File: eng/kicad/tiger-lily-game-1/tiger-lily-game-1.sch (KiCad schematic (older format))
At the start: 11 parts, among them J1 Conn_01x06_Male, SW1 SW_Push, SW2 SW_Push, SW3 SW_Push, SW4 SW_SPDT, U1 PIC16F1454-IP

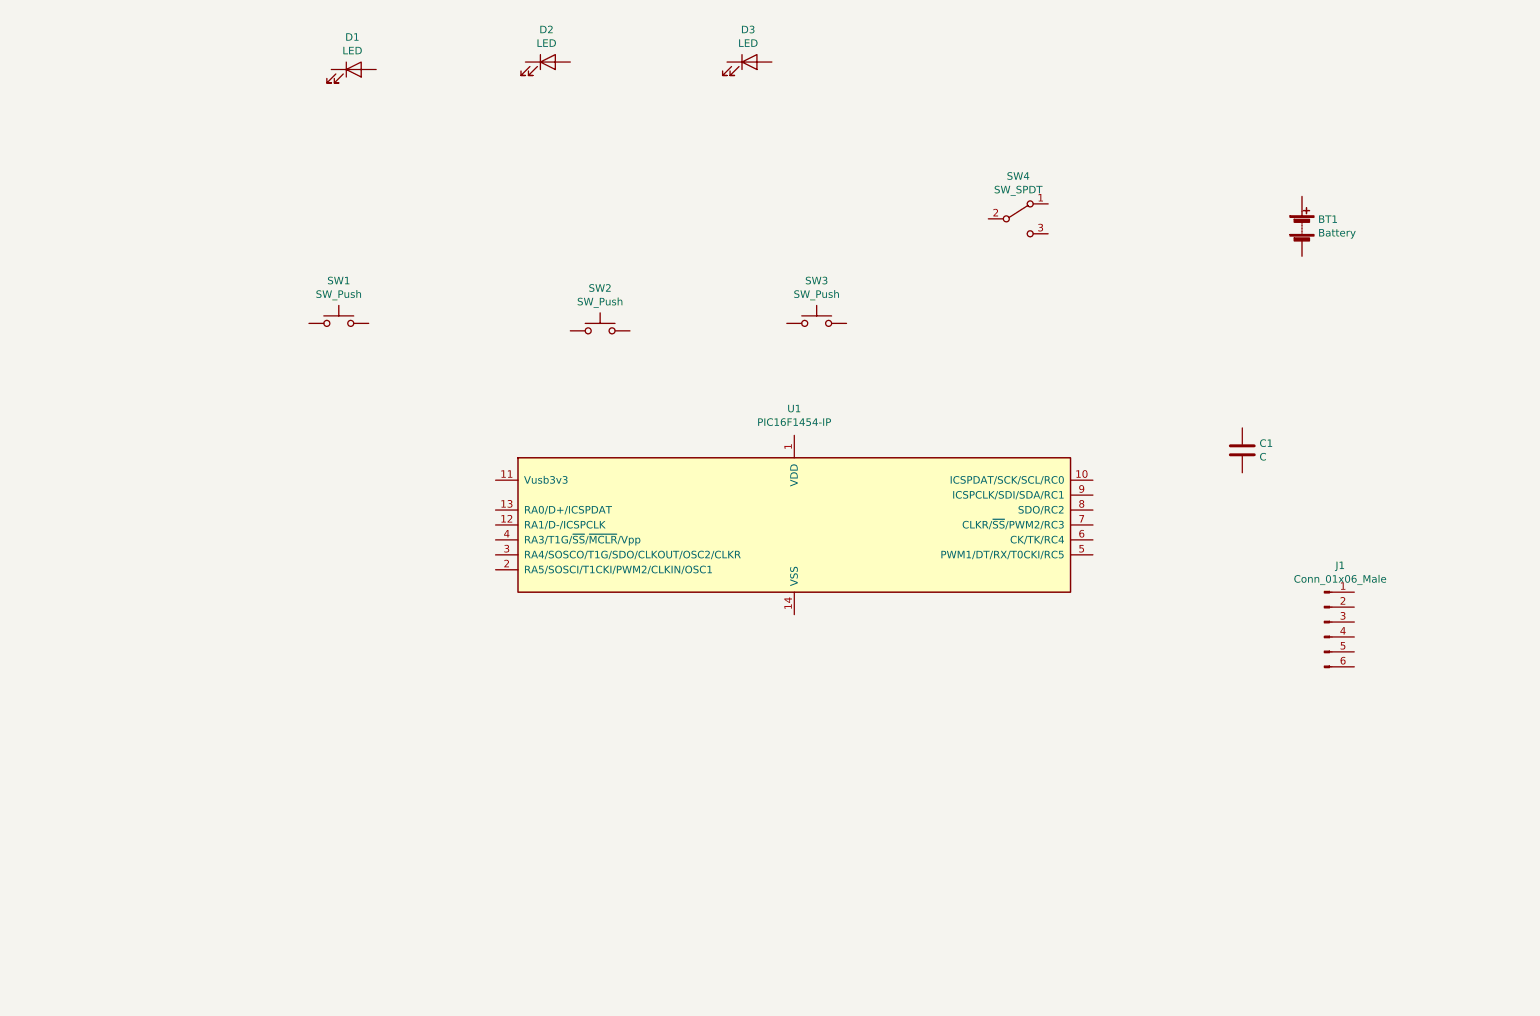
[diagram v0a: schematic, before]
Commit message: Changed MCU to PIC16F15323 as simpler, cheaper, and available. Added custom schematic for MCU as not in library installed. Tried PCB layout (do not like it so will change). Added skeleton firmware project files.
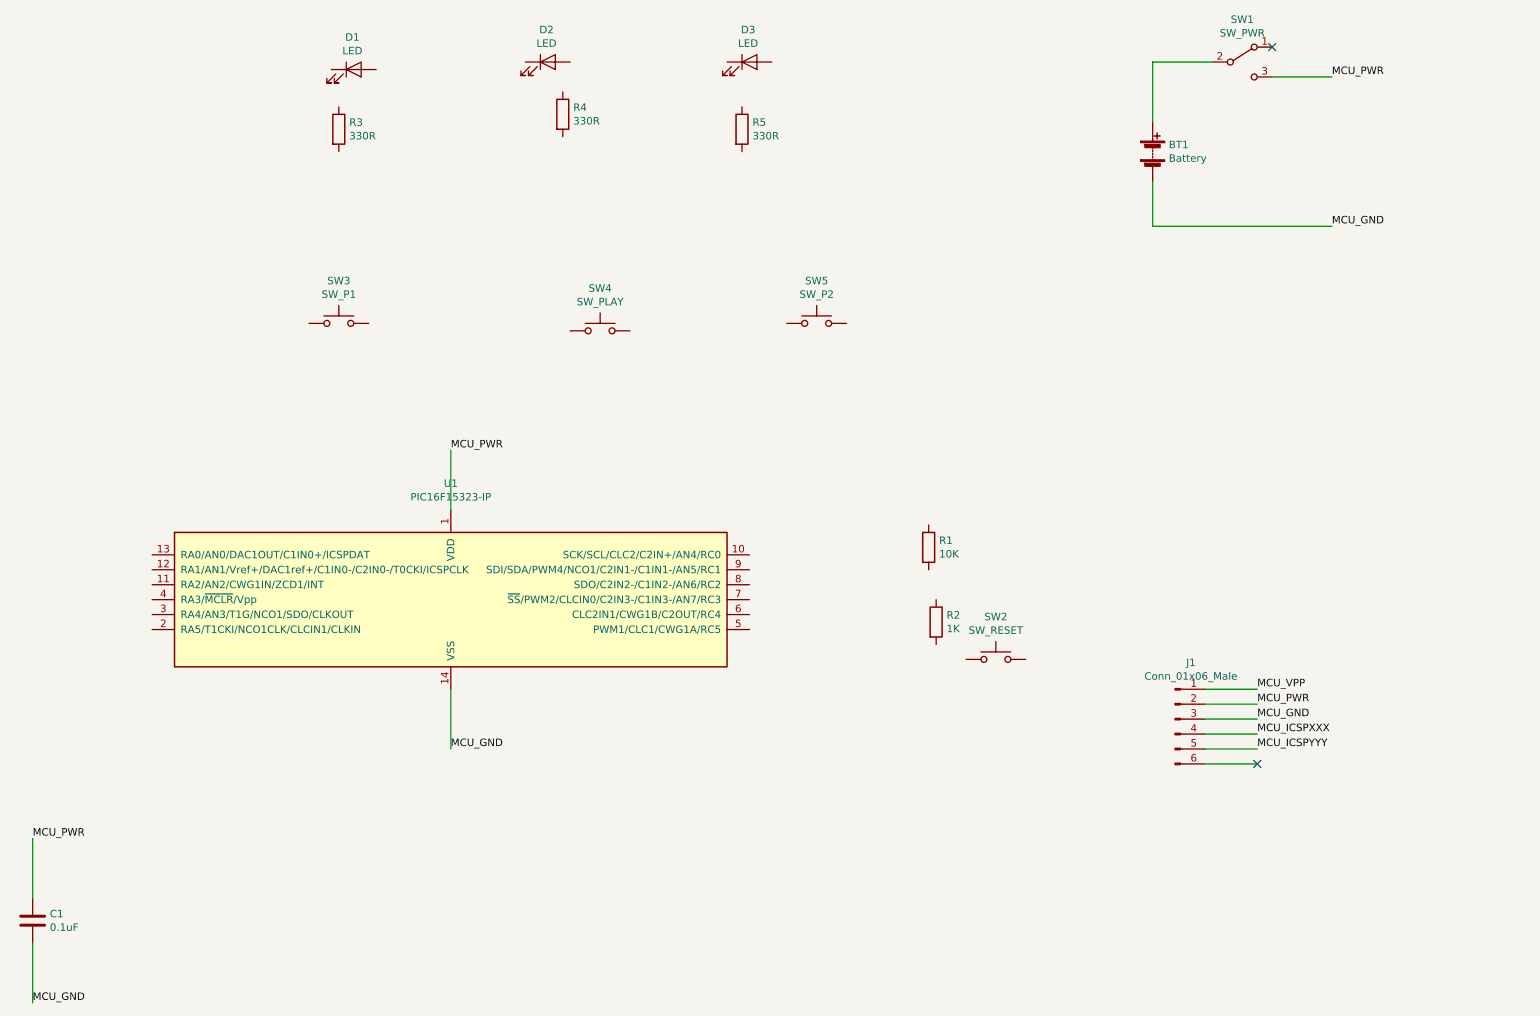
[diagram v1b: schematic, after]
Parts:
- removed U1: PIC16F1454-IP, Package_DIP:DIP-14_W7.62mm_Socket, symbol MCU_Microchip_PIC16:PIC16F1454-IP
- added R1: 10K, Resistor_THT:R_Axial_DIN0204_L3.6mm_D1.6mm_P7.62mm_Horizontal, symbol Device:R
- added R2: 1K, Resistor_THT:R_Axial_DIN0204_L3.6mm_D1.6mm_P7.62mm_Horizontal, symbol Device:R
- added R3, R4, R5: 330R, Resistor_THT:R_Axial_DIN0204_L3.6mm_D1.6mm_P7.62mm_Horizontal, symbol Device:R
- added SW2: SW_RESET, Button_Switch_THT:SW_PUSH_6mm, symbol Switch:SW_Push
- added U1: PIC16F15323-IP, Package_DIP:DIP-14_W7.62mm, symbol MCU_Microchip_PIC16(L)F15313_23:PIC16F15323-IP
- C1: value C -> 0.1uF
- SW1: renamed from SW4; value SW_SPDT -> SW_PWR
- SW3: renamed from SW1; value SW_Push -> SW_P1
- SW4: renamed from SW2; value SW_Push -> SW_PLAY
- SW5: renamed from SW3; value SW_Push -> SW_P2
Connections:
- net at BT1.1 (+): now also SW1.2 (B)
- net MCU_GND: now reaches BT1.2 (-)
- net MCU_GND: now also C1.2, J1.3 (Pin_3), U1.14 (VSS)
- net MCU_PWR: now reaches C1.1
- net MCU_PWR: now also J1.2 (Pin_2), SW1.3 (C), U1.1 (VDD)
- net MCU_VPP: now reaches J1.1 (Pin_1)
- net MCU_ICSPXXX: now reaches J1.4 (Pin_4)
- net MCU_ICSPYYY: now reaches J1.5 (Pin_5)
- no-connect marks 0 -> 2
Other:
- moved on the sheet: BT1, C1, J1, SW1
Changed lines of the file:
@@
 EESchema Schematic File Version 4
+LIBS:tiger-lily-game-1-cache
 EELAYER 26 0
 EELAYER END
@@
 $EndDescr
 $Comp
-L Switch:SW_Push SW1
+L Switch:SW_Push SW3
 U 1 1 61758FB1
 P 2950 2850
-F 0 "SW1" H 2950 3135 50  0000 C CNN
-F 1 "SW_Push" H 2950 3044 50  0000 C CNN
+F 0 "SW3" H 2950 3135 50  0000 C CNN
+F 1 "SW_P1" H 2950 3044 50  0000 C CNN
 F 2 "Button_Switch_THT:SW_PUSH_6mm" H 2950 3050 50  0001 C CNN
 F 3 "" H 2950 3050 50  0001 C CNN
@@
 $EndComp
 $Comp
-L Switch:SW_Push SW2
+L Switch:SW_Push SW4
 U 1 1 6175903E
 P 4700 2900
-F 0 "SW2" H 4700 3185 50  0000 C CNN
-F 1 "SW_Push" H 4700 3094 50  0000 C CNN
+F 0 "SW4" H 4700 3185 50  0000 C CNN
+F 1 "SW_PLAY" H 4700 3094 50  0000 C CNN
 F 2 "Button_Switch_THT:SW_PUSH_6mm" H 4700 3100 50  0001 C CNN
 F 3 "" H 4700 3100 50  0001 C CNN
@@
 $EndComp
 $Comp
-L Switch:SW_Push SW3
+L Switch:SW_Push SW5
 U 1 1 6175906C
 P 6150 2850
-F 0 "SW3" H 6150 3135 50  0000 C CNN
-F 1 "SW_Push" H 6150 3044 50  0000 C CNN
+F 0 "SW5" H 6150 3135 50  0000 C CNN
+F 1 "SW_P2" H 6150 3044 50  0000 C CNN
 F 2 "Button_Switch_THT:SW_PUSH_6mm" H 6150 3050 50  0001 C CNN
 F 3 "" H 6150 3050 50  0001 C CNN
@@
 L Device:Battery BT1
 U 1 1 6175958B
-P 9400 2200
-F 0 "BT1" H 9508 2246 50  0000 L CNN
-F 1 "Battery" H 9508 2155 50  0000 L CNN
-F 2 "Battery:BatteryHolder_Keystone_2468_2xAAA" V 9400 2260 50  0001 C CNN
-F 3 "~" V 9400 2260 50  0001 C CNN
-	1    9400 2200
-	1    0    0    -1
-$EndComp
-$Comp
-L MCU_Microchip_PIC16:PIC16F1454-IP U1
-U 1 1 61759CA8
-P 6000 4200
-F 0 "U1" H 6000 4978 50  0000 C CNN
-F 1 "PIC16F1454-IP" H 6000 4887 50  0000 C CNN
-F 2 "Package_DIP:DIP-14_W7.62mm_Socket" H 6000 4200 50  0001 C CNN
-F 3 "http://ww1.microchip.com/downloads/en/DeviceDoc/41639A.pdf" H 6000 4200 50  0001 C CNN
-	1    6000 4200
+P 8400 1700
+F 0 "BT1" H 8508 1746 50  0000 L CNN
+F 1 "Battery" H 8508 1655 50  0000 L CNN
+F 2 "Battery:BatteryHolder_Keystone_2468_2xAAA" V 8400 1760 50  0001 C CNN
+F 3 "~" V 8400 1760 50  0001 C CNN
+	1    8400 1700
 	1    0    0    -1
 $EndComp
@@
 L Device:C C1
 U 1 1 61759DDE
-P 9000 3700
-F 0 "C1" H 9115 3746 50  0000 L CNN
-F 1 "C" H 9115 3655 50  0000 L CNN
-F 2 "Capacitor_THT:C_Disc_D3.0mm_W2.0mm_P2.50mm" H 9038 3550 50  0001 C CNN
-F 3 "~" H 9000 3700 50  0001 C CNN
-	1    9000 3700
+P 900 6850
+F 0 "C1" H 1015 6896 50  0000 L CNN
+F 1 "0.1uF" H 1015 6805 50  0000 L CNN
+F 2 "Capacitor_THT:C_Disc_D3.0mm_W2.0mm_P2.50mm" H 938 6700 50  0001 C CNN
+F 3 "~" H 900 6850 50  0001 C CNN
+	1    900  6850
 	1    0    0    -1
 $EndComp
@@
 L Connector:Conn_01x06_Male J1
 U 1 1 6175A655
-P 9550 4850
-F 0 "J1" H 9656 5228 50  0000 C CNN
-F 1 "Conn_01x06_Male" H 9656 5137 50  0000 C CNN
-F 2 "Connector_PinHeader_2.54mm:PinHeader_1x06_P2.54mm_Horizontal" H 9550 4850 50  0001 C CNN
-F 3 "~" H 9550 4850 50  0001 C CNN
-	1    9550 4850
-	1    0    0    -1
-$EndComp
-$Comp
-L Switch:SW_SPDT SW4
+P 8550 5500
+F 0 "J1" H 8656 5878 50  0000 C CNN
+F 1 "Conn_01x06_Male" H 8656 5787 50  0000 C CNN
+F 2 "Connector_PinHeader_2.54mm:PinHeader_1x06_P2.54mm_Horizontal" H 8550 5500 50  0001 C CNN
+F 3 "~" H 8550 5500 50  0001 C CNN
+	1    8550 5500
+	1    0    0    -1
+$EndComp
+$Comp
+L Switch:SW_SPDT SW1
 U 1 1 6175AAD5
-P 7500 2150
-F 0 "SW4" H 7500 2435 50  0000 C CNN
-F 1 "SW_SPDT" H 7500 2344 50  0000 C CNN
-F 2 "Button_Switch_THT:SW_CuK_OS102011MA1QN1_SPDT_Angled" H 7500 2150 50  0001 C CNN
-F 3 "" H 7500 2150 50  0001 C CNN
-	1    7500 2150
-	1    0    0    -1
-$EndComp
+P 9000 1100
+F 0 "SW1" H 9000 1385 50  0000 C CNN
+F 1 "SW_PWR" H 9000 1294 50  0000 C CNN
+F 2 "Button_Switch_THT:SW_CuK_OS102011MA1QN1_SPDT_Angled" H 9000 1100 50  0001 C CNN
+F 3 "" H 9000 1100 50  0001 C CNN
+	1    9000 1100
+	1    0    0    -1
+$EndComp
+$Comp
+L MCU_Microchip_PIC16(L)F15313_23:PIC16F15323-IP U1
+U 1 1 61761BE8
+P 3700 4700
+F 0 "U1" H 3700 5478 50  0000 C CNN
+F 1 "PIC16F15323-IP" H 3700 5387 50  0000 C CNN
+F 2 "Package_DIP:DIP-14_W7.62mm" H 3700 4700 50  0001 C CNN
+F 3 "http://ww1.microchip.com/downloads/en/DeviceDoc/41607A.pdf" H 3700 4700 50  0001 C CNN
+	1    3700 4700
+	1    0    0    -1
+$EndComp
+Wire Wire Line
+	3700 5300 3700 5700
+Text Label 3700 5700 0    50   ~ 0
+MCU_GND
+Text Label 3700 3700 0    50   ~ 0
+MCU_PWR
+Wire Wire Line
+	3700 3700 3700 4100
+Wire Wire Line
+	900  7000 900  7400
+Text Label 900  7400 0    50   ~ 0
+MCU_GND
+Text Label 900  6300 0    50   ~ 0
+MCU_PWR
+Wire Wire Line
+	900  6300 900  6700
+Wire Wire Line
+	8750 5300 9100 5300
+Wire Wire Line
+	8750 5400 9100 5400
+Wire Wire Line
+	8750 5500 9100 5500
+Wire Wire Line
+	8750 5600 9100 5600
+Wire Wire Line
+	8750 5700 9100 5700
+Wire Wire Line
+	8750 5800 9100 5800
+Text Label 9100 5400 0    50   ~ 0
+MCU_PWR
+Text Label 9100 5500 0    50   ~ 0
+MCU_GND
+Text Label 9100 5300 0    50   ~ 0
+MCU_VPP
+Text Label 9100 5600 0    50   ~ 0
+MCU_ICSPXXX
+Text Label 9100 5700 0    50   ~ 0
+MCU_ICSPYYY
+NoConn ~ 9100 5800
+$Comp
+L Device:R R1
+U 1 1 6176251C
+P 6900 4350
+F 0 "R1" H 6970 4396 50  0000 L CNN
+F 1 "10K" H 6970 4305 50  0000 L CNN
+F 2 "Resistor_THT:R_Axial_DIN0204_L3.6mm_D1.6mm_P7.62mm_Horizontal" V 6830 4350 50  0001 C CNN
+F 3 "~" H 6900 4350 50  0001 C CNN
+	1    6900 4350
+	1    0    0    -1
+$EndComp
+$Comp
+L Device:R R2
+U 1 1 6176263C
+P 6950 4850
+F 0 "R2" H 7020 4896 50  0000 L CNN
+F 1 "1K" H 7020 4805 50  0000 L CNN
+F 2 "Resistor_THT:R_Axial_DIN0204_L3.6mm_D1.6mm_P7.62mm_Horizontal" V 6880 4850 50  0001 C CNN
+F 3 "~" H 6950 4850 50  0001 C CNN
+	1    6950 4850
+	1    0    0    -1
+$EndComp
+$Comp
+L Switch:SW_Push SW2
+U 1 1 6176271D
+P 7350 5100
+F 0 "SW2" H 7350 5385 50  0000 C CNN
+F 1 "SW_RESET" H 7350 5294 50  0000 C CNN
+F 2 "Button_Switch_THT:SW_PUSH_6mm" H 7350 5300 50  0001 C CNN
+F 3 "" H 7350 5300 50  0001 C CNN
+	1    7350 5100
+	1    0    0    -1
+$EndComp
+$Comp
+L Device:R R3
+U 1 1 617627B7
+P 2950 1550
+F 0 "R3" H 3020 1596 50  0000 L CNN
+F 1 "330R" H 3020 1505 50  0000 L CNN
+F 2 "Resistor_THT:R_Axial_DIN0204_L3.6mm_D1.6mm_P7.62mm_Horizontal" V 2880 1550 50  0001 C CNN
+F 3 "~" H 2950 1550 50  0001 C CNN
+	1    2950 1550
+	1    0    0    -1
+$EndComp
+$Comp
+L Device:R R4
+U 1 1 61762827
+P 4450 1450
+F 0 "R4" H 4520 1496 50  0000 L CNN
+F 1 "330R" H 4520 1405 50  0000 L CNN
+F 2 "Resistor_THT:R_Axial_DIN0204_L3.6mm_D1.6mm_P7.62mm_Horizontal" V 4380 1450 50  0001 C CNN
+F 3 "~" H 4450 1450 50  0001 C CNN
+	1    4450 1450
+	1    0    0    -1
+$EndComp
+$Comp
+L Device:R R5
+U 1 1 617628A8
+P 5650 1550
+F 0 "R5" H 5720 1596 50  0000 L CNN
+F 1 "330R" H 5720 1505 50  0000 L CNN
+F 2 "Resistor_THT:R_Axial_DIN0204_L3.6mm_D1.6mm_P7.62mm_Horizontal" V 5580 1550 50  0001 C CNN
+F 3 "~" H 5650 1550 50  0001 C CNN
+	1    5650 1550
+	1    0    0    -1
+$EndComp
+Wire Wire Line
+	8400 1500 8400 1100
+Wire Wire Line
+	8400 1100 8800 1100
+Wire Wire Line
+	8400 1900 8400 2200
+Wire Wire Line
+	8400 2200 9600 2200
+Wire Wire Line
+	9200 1200 9600 1200
+NoConn ~ 9200 1000
+Text Label 9600 1200 0    50   ~ 0
+MCU_PWR
+Text Label 9600 2200 0    50   ~ 0
+MCU_GND
 $EndSCHEMATC

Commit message: Schematic and PCB design (WIP). Firmware (WIP). Checked in for backup.
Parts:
- added R6, R7, R8: 330R, Resistor_THT:R_Axial_DIN0204_L3.6mm_D1.6mm_P7.62mm_Horizontal, symbol Device:R
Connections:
- net MCU_GND: now also SW2.1, R6.2, R7.2, R8.2
- net MCU_ICSPXXX: now also U1.13 (RA0/AN0/DAC1OUT/C1IN0+/ICSPDAT)
- net MCU_ICSPYYY: now also U1.12 (RA1/AN1/Vref+/DAC1ref+/C1IN0-/C2IN0-/T0CKI/ICSPCLK)
- net MCU_PWR: now also R1.1, R3.1, R4.1, R5.1
- net MCU_VPP: now also R2.1, U1.4 (RA3/~MCLR~/Vpp)
- net at SW3.1: now also R6.1
- net SW_P1: now reaches SW3.2
- net SW_P1: now also U1.7 (~SS~/PWM2/CLCIN0/C2IN3-/C1IN3-/AN7/RC3)
- net at SW4.1: now also R7.1
- net SW_GO: now reaches SW4.2
- net SW_GO: now also U1.6 (CLC2IN1/CWG1B/C2OUT/RC4)
- net at SW5.1: now also R8.1
- net SW_P2: now reaches SW5.2
- net SW_P2: now also U1.5 (PWM1/CLC1/CWG1A/RC5)
- net LED_P1: now reaches D1.1 (K)
- net LED_P1: now also U1.10 (SCK/SCL/CLC2/C2IN+/AN4/RC0)
- net at D1.2 (A): now also R3.2
- net LED_GO: now reaches D2.1 (K)
- net LED_GO: now also U1.9 (SDI/SDA/PWM4/NCO1/C2IN1-/C1IN1-/AN5/RC1)
- net at D2.2 (A): now also R4.2
- net LED_P2: now reaches D3.1 (K)
- net LED_P2: now also U1.8 (SDO/C2IN2-/C1IN2-/AN6/RC2)
- net at D3.2 (A): now also R5.2
- net at R1.2: now also R2.2, SW2.2
- no-connect marks 2 -> 5
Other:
- moved on the sheet: BT1, D1, D2, D3, J1, R1, R2, R3, R4, R5, SW1, SW2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

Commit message: Candidate Schematic and PCB. TODO: Check silkscreen text.
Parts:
- BT1: footprint Battery:BatteryHolder_Keystone_2468_2xAAA -> Battery:BatteryHolder_Keystone_2479_3xAAA
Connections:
- net SW_P1: now also U1.5 (PWM1/CLC1/CWG1A/RC5); no longer U1.7 (~SS~/PWM2/CLCIN0/C2IN3-/C1IN3-/AN7/RC3)
- net SW_P2: now also U1.7 (~SS~/PWM2/CLCIN0/C2IN3-/C1IN3-/AN7/RC3); no longer U1.5 (PWM1/CLC1/CWG1A/RC5)
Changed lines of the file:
@@
 F 0 "BT1" H 9408 1746 50  0000 L CNN
 F 1 "Battery" H 9408 1655 50  0000 L CNN
-F 2 "Battery:BatteryHolder_Keystone_2468_2xAAA" V 9300 1760 50  0001 C CNN
+F 2 "Battery:BatteryHolder_Keystone_2479_3xAAA" V 9300 1760 50  0001 C CNN
 F 3 "~" V 9300 1760 50  0001 C CNN
 	1    9300 1700
@@
 Wire Wire Line
 	6250 1050 6250 1400
-Text Label 6050 4700 0    50   ~ 0
+Text Label 6050 4900 0    50   ~ 0
 SW_P1
 Text Label 6050 4800 0    50   ~ 0
 SW_GO
-Text Label 6050 4900 0    50   ~ 0
+Text Label 6050 4700 0    50   ~ 0
 SW_P2
 Text Label 5050 1050 0    50   ~ 0
